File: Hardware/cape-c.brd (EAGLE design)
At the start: 134 x 145.5 mm, 93 parts, among them IC1 74VHC541, IC2 74VHC541, IC3 74VHC541, IC4 74VHC541, IC5 74VHC541, IC6 74VHC541, IC7 74VHC541, IC8 74VHC541, IC9 74VHC541, J1 MOLEX-P4, J2 RJ45-8P8C-16FCI-16, J3 RJ45-8P8C-16FCI-16, Q1 N-MOSFET-DUALSO8, Q10 N-MOSFET-DUALSO8, Q11 N-MOSFET-DUALSO8, Q12 N-MOSFET-DUALSO8, Q13 N-MOSFET-DUALSO8, Q14 N-MOSFET-DUALSO8, Q15 N-MOSFET-DUALSO8, Q16 N-MOSFET-DUALSO8, Q2 N-MOSFET-DUALSO8, Q3 N-MOSFET-DUALSO8, Q4 N-MOSFET-DUALSO8, Q5 N-MOSFET-DUALSO8, Q6 N-MOSFET-DUALSO8, Q7 N-MOSFET-DUALSO8, Q8 N-MOSFET-DUALSO8, Q9 N-MOSFET-DUALSO8

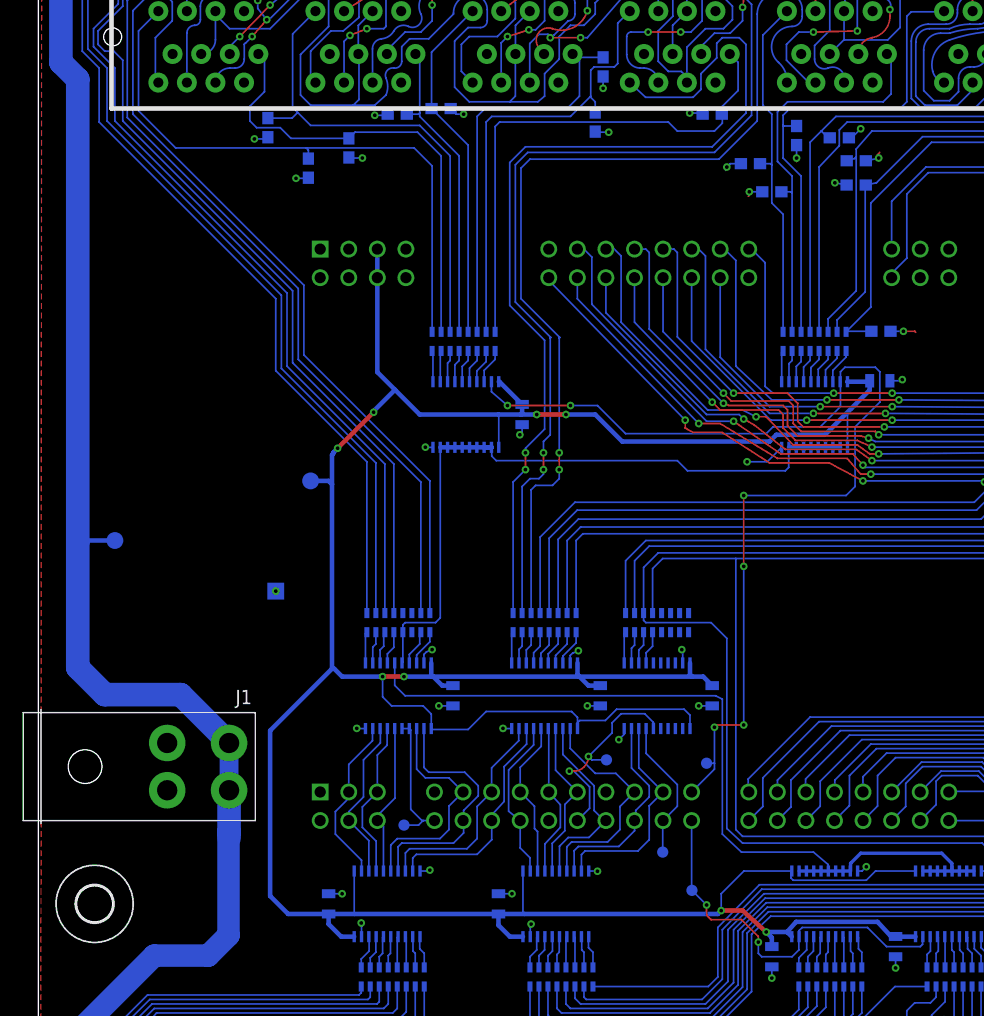
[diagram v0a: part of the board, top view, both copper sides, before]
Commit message: Replaced 5v rail with 3.3v rail (fixes #13)
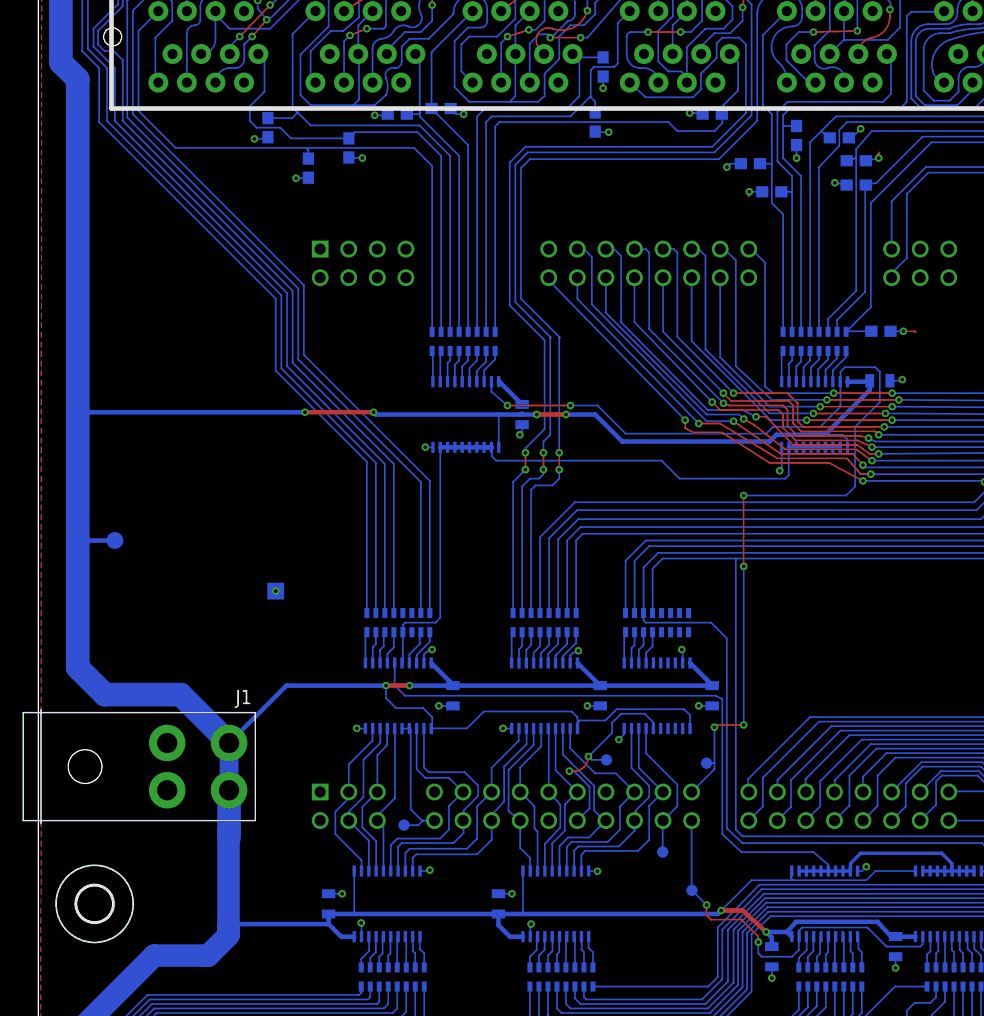
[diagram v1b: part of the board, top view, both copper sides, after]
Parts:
- removed VCC5V_TP: PTR1TP15R, tenna_avr_AD7021_v0_9_shrink:TP15R
- C1, C2, C20, C21, C3, C4, C5, C6, C7: value 1uF -> 0.1uF
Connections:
- removed net VCC5V: C1.1, C2.1, C20.1, C21.1, C3.1, C4.1, C5.1, C6.1, C7.1, IC1.1, IC1.20, IC2.1, IC2.20, IC3.1, IC3.20, IC4.1, IC4.20, IC5.1, IC5.20, IC6.1, IC6.20, IC7.1, IC7.20, IC8.1, IC8.20, IC9.1, IC9.20, U$1.51, U$1.52, VCC5V_TP.TP
- new net VDD_5V: U$1.51, U$1.52
- net VCC3V3: now also C1.1, C2.1, C20.1, C21.1, C3.1, C4.1, C5.1, C6.1, C7.1, IC1.1, IC1.20, IC2.1, IC2.20, IC3.1, IC3.20, IC4.1, IC4.20, IC5.1, IC5.20, IC6.1, IC6.20, IC7.1, IC7.20, IC8.1, IC8.20, IC9.1, IC9.20
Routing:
- net VCC5V: track 299.1 -> 0.00 mm, vias 8 -> 0
- net VCC3V3: track 755.4 -> 1027.6 mm, vias 38 -> 46
- net GND: track 128.5 -> 127.1 mm
- net SCL_BUF_A: track 61.6 -> 62.6 mm
